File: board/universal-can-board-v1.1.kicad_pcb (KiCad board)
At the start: 2 copper layers, 49.5 x 111.8 mm, 70 parts, among them IC1 ATMEGA328P-A, P1 USB_OTG, P2 CONN_01X08, P3 CONN_01X02, P4 CONN_01X08, P5 CONN_01X08, U1 FT232RL, U2 LM1117-3.3, U3 MCP2515-I/ST, U4 MCP2551-I/SN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

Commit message: Just saved new pcb layout try.
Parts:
- D10, D11, D12, D13, D14, D4, D5, D6, D7, D8, D9, R10, R11, R12, R13, R14, R7, R8, R9, U1, U4: moved to B.Cu
- moved C23 91.0 mm to (244.3, 119.9)
- moved C25 91.0 mm to (245.4, 125.0)
- moved R15 91.0 mm to (238.3, 130.0)
- moved R5 91.0 mm to (246.9, 115.8)
- moved C24 91.0 mm to (239.5, 152.4)
- moved C9 91.0 mm to (251.0, 144.8)
- moved R16 91.0 mm to (234.2, 125.5)
- moved U4 70.2 mm to (145.3, 57.9), turned to 0 degrees
- moved Y2 68.8 mm to (141.7, 68.1), turned to 90 degrees
- moved C5 68.8 mm to (230.1, 95.0)
- moved R2 68.8 mm to (225.0, 101.1)
- moved R4 68.8 mm to (225.0, 96.0)
- moved R3 64.8 mm to (215.4, 46.7)
- moved C21 57.9 mm to (143.3, 97.0), turned to 180 degrees
- moved P4 54.9 mm to (156.0, 80.3), turned to 90 degrees
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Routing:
- net Net-(C20-Pad1): track 92.5 -> 0.00 mm, vias 2 -> 0
- net VCC: track 57.5 -> 0.00 mm, vias 2 -> 0
- net +5V: track 46.3 -> 0.00 mm, vias 1 -> 0
- net Net-(D14-Pad2): track 45.8 -> 0.00 mm
- net Net-(P4-Pad5): track 37.9 -> 0.00 mm, vias 1 -> 0
- net Net-(P4-Pad4): track 29.1 -> 0.00 mm
- net Net-(U3-Pad2): track 16.3 -> 0.00 mm
- net USB_D-: track 15.9 -> 0.00 mm
- net USB_D+: track 15.7 -> 0.00 mm, vias 2 -> 0
- net Net-(U3-Pad9): track 10.9 -> 0.00 mm
- net Net-(U3-Pad1): track 6.75 -> 0.00 mm
- net Net-(U3-Pad8): track 5.24 -> 0.00 mm
- net RESET: track 3.28 -> 0.00 mm
- net Net-(R15-Pad1): track 2.78 -> 0.00 mm
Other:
- board outline removed

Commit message: Moved on with the layout.
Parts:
- C1, C4, R16, R2, R3: moved to B.Cu
- D13, D14, D4: moved to F.Cu
- moved C9 122.0 mm to (138.7, 97.0)
- moved R15 115.8 mm to (152.4, 52.3)
- moved C24 115.2 mm to (136.1, 101.6)
- moved R16 112.5 mm to (148.3, 52.8), turned to 180 degrees
- moved C23 111.1 mm to (148.3, 64.0), turned to 0 degrees
- moved C25 107.7 mm to (149.4, 76.2)
- moved R5 103.4 mm to (145.3, 96.5)
- moved R3 88.0 mm to (144.3, 98.6), turned to 90 degrees
- moved R4 83.0 mm to (144.3, 115.3)
- moved C4 79.7 mm to (145.3, 103.6), turned to 270 degrees
- moved R2 78.3 mm to (146.8, 98.6), turned to 270 degrees
- moved C5 77.9 mm to (152.4, 89.9), turned to 270 degrees
- moved C3 74.9 mm to (138.7, 86.9), turned to 90 degrees
- moved D3 65.6 mm to (150.9, 117.3)
- moved R6 65.4 mm to (158.0, 116.3)
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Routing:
- net IO7: track 0.00 -> 58.2 mm, vias 0 -> 3
- net IO5: track 0.00 -> 52.8 mm, vias 0 -> 5
- net IO6: track 0.00 -> 50.7 mm, vias 0 -> 3
- net Net-(D14-Pad2): track 0.00 -> 50.1 mm, vias 0 -> 1
- net IO4: track 0.00 -> 44.2 mm, vias 0 -> 3
- net VCC: track 0.00 -> 34.2 mm, vias 0 -> 2
- net +5V: track 0.00 -> 33.8 mm
- net IO2: track 0.00 -> 33.1 mm, vias 0 -> 3
- net IO1: track 0.00 -> 27.0 mm, vias 0 -> 3
- net IO0: track 0.00 -> 19.5 mm, vias 0 -> 1
- net CAN_INT: track 0.00 -> 18.0 mm, vias 0 -> 2
- net CAN_SO: track 0.00 -> 13.4 mm, vias 0 -> 2
- net Net-(U3-Pad1): track 0.00 -> 12.6 mm, vias 0 -> 1
- net Net-(C20-Pad1): track 0.00 -> 12.2 mm
- net Net-(U3-Pad2): track 0.00 -> 11.6 mm, vias 0 -> 1
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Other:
- board outline added: 49.3 x 59.4 mm

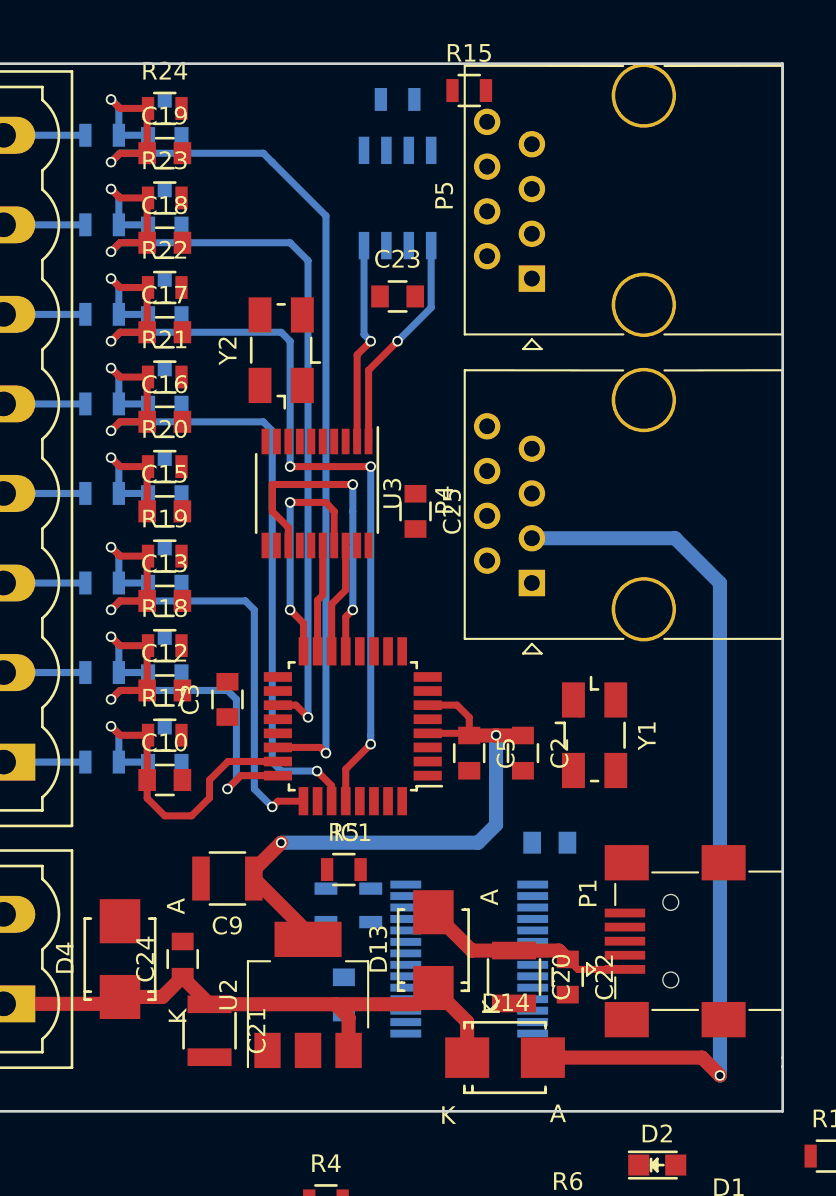
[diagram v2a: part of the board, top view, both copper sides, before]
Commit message: Routing of board v1.1
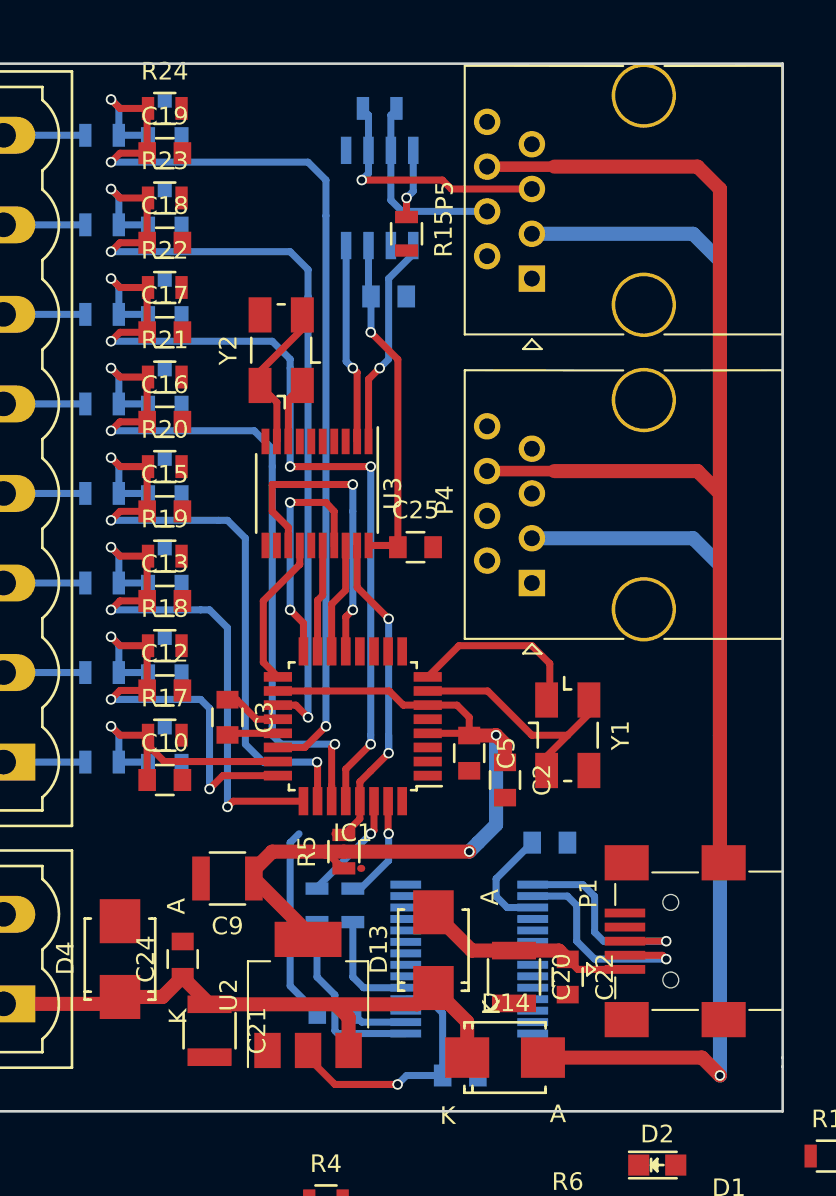
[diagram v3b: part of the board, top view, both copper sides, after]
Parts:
- added C6: 100n, Capacitors_SMD:C_0805, B.Cu at (151.9, 108.2)
- C23: moved to B.Cu
- moved R15 8.87 mm to (148.8, 60.5), turned to 270 degrees
- moved R2 3.05 mm to (143.8, 98.6)
- moved C25 2.03 mm to (149.4, 78.2), turned to 0 degrees
- moved C2 1.83 mm to (154.4, 91.4)
- moved R3 1.52 mm to (145.8, 98.6)
- moved Y1 1.52 mm to (158.0, 88.9)
- moved R16 1.14 mm to (147.3, 53.3)
- moved C4 1.14 mm to (144.8, 104.6), turned to 0 degrees
- moved U4 1.02 mm to (147.3, 58.4)
- moved C3 1.02 mm to (138.7, 87.9), turned to 270 degrees
- moved R5 1.02 mm to (145.3, 95.5), turned to 90 degrees
- moved C23 0.51 mm to (147.8, 64.0)
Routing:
- net GND: track 0.00 -> 68.7 mm
- net VCC: track 34.2 -> 79.1 mm, vias 2 -> 4
- net RESET: track 0.00 -> 30.8 mm, vias 0 -> 2
- net Net-(D14-Pad2): track 50.1 -> 79.3 mm
- net IO3: track 8.75 -> 37.4 mm, vias 1 -> 3
- net Net-(P4-Pad5): track 0.00 -> 14.2 mm, vias 0 -> 1
- net Net-(IC1-Pad7): track 0.00 -> 14.0 mm
- net USB_D-: track 0.00 -> 12.7 mm, vias 0 -> 1
- net USB_D+: track 0.00 -> 12.4 mm, vias 0 -> 1
- net Net-(P4-Pad4): track 0.00 -> 11.1 mm
- net USB_RX: track 0.00 -> 10.7 mm
- net Net-(IC1-Pad8): track 0.80 -> 10.2 mm
- net CAN_SCK: track 0.00 -> 8.66 mm
- net Net-(U3-Pad9): track 0.00 -> 8.57 mm
- net USB_TX: track 0.00 -> 6.37 mm
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
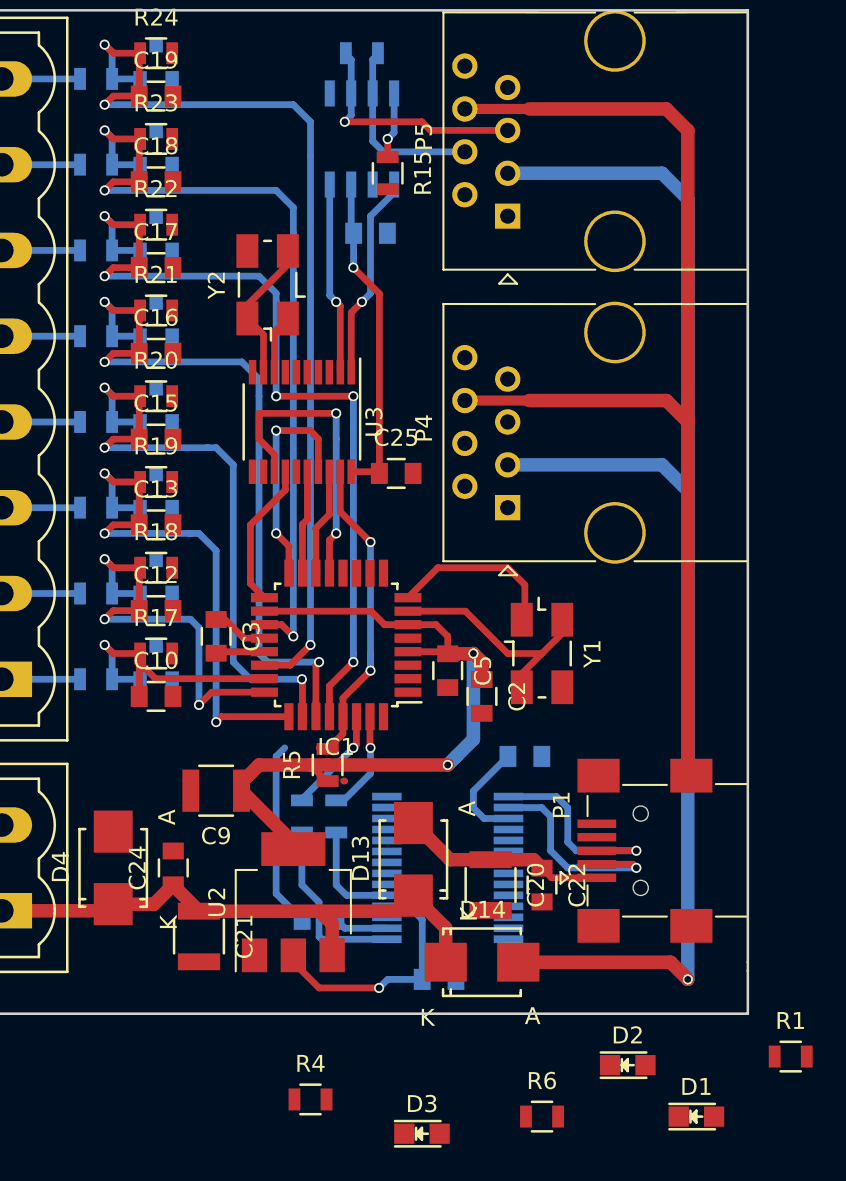
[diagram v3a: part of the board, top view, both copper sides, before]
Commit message: Routing of PCB v1.1. All parts are placed now.
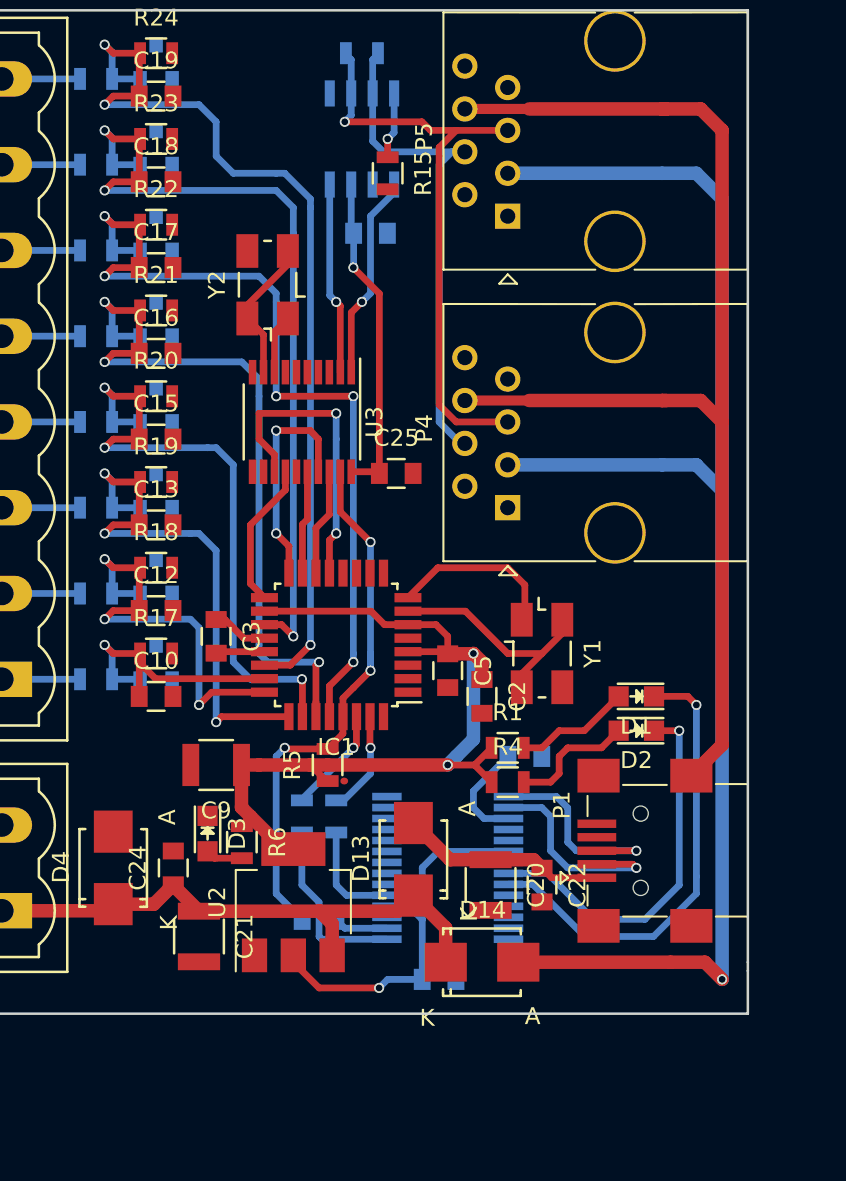
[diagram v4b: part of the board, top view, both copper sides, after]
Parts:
- moved D1 25.1 mm to (163.6, 91.4), turned to 180 degrees
- moved R1 24.8 mm to (156.0, 94.5)
- moved R6 24.1 mm to (140.2, 100.1), turned to 270 degrees
- moved R4 22.1 mm to (156.0, 96.5)
- moved D3 21.8 mm to (138.2, 99.6), turned to 270 degrees
- moved D2 19.8 mm to (163.6, 93.5), turned to 180 degrees
- moved C9 1.52 mm to (138.7, 95.5)
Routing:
- net Net-(D1-Pad1): track 0.00 -> 27.4 mm, vias 0 -> 1
- net Net-(D2-Pad1): track 0.00 -> 22.7 mm, vias 0 -> 1
- net Net-(P4-Pad5): track 14.2 -> 35.4 mm
- net Net-(P4-Pad4): track 11.1 -> 30.2 mm
- net VCC: track 79.1 -> 94.2 mm
- net Net-(D2-Pad2): track 0.00 -> 7.48 mm
- net Net-(D1-Pad2): track 0.00 -> 6.88 mm
- net Net-(D14-Pad2): track 79.3 -> 85.4 mm
- net GND: track 68.7 -> 74.2 mm
- net RESET: track 30.8 -> 33.3 mm, vias 2 -> 3
- net Net-(D3-Pad2): track 0.00 -> 2.20 mm
- net IO7: track 57.8 -> 56.3 mm

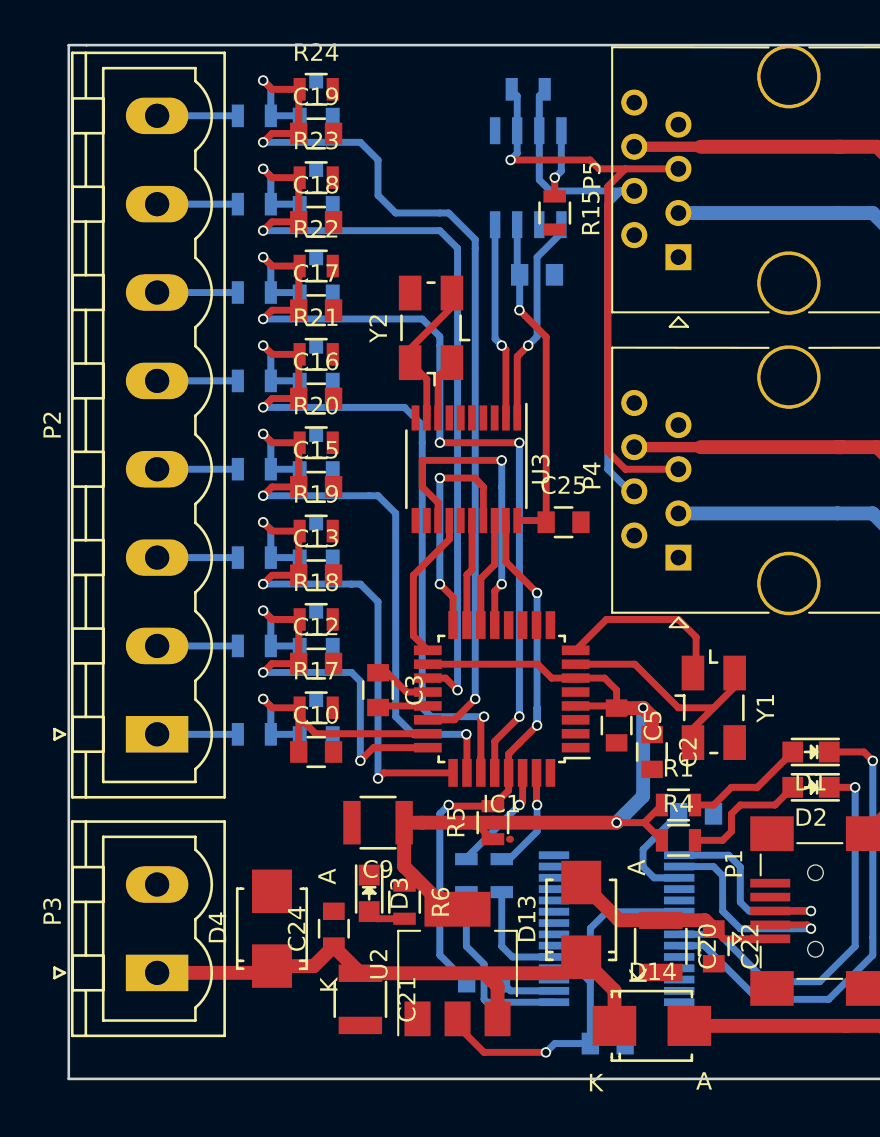
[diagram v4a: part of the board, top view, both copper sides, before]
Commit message: Updated board layout.
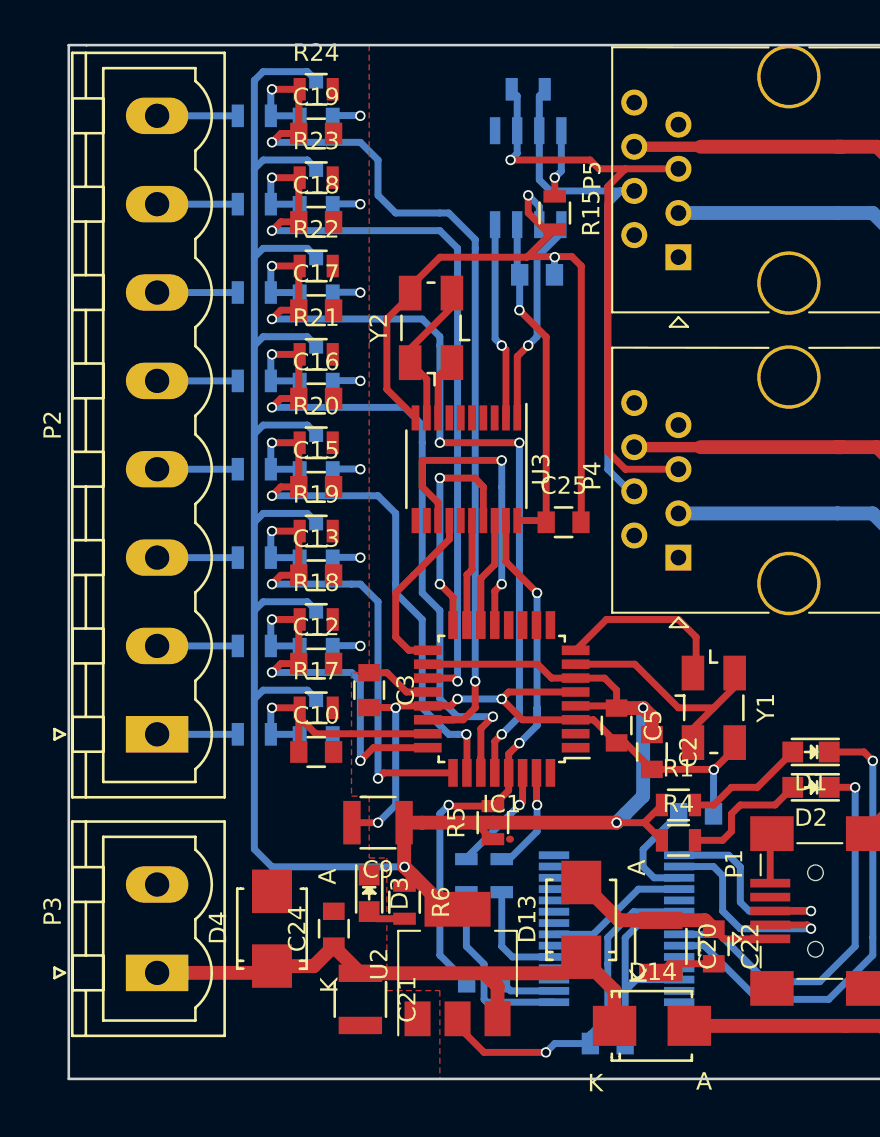
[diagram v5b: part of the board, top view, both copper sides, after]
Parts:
- moved C3 0.51 mm to (138.2, 87.9)
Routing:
- net GND: track 74.2 -> 192.2 mm, vias 0 -> 14
- net VCC: track 94.2 -> 176.2 mm, vias 4 -> 5
- net IO3: track 37.4 -> 34.0 mm
- net IO6: track 50.0 -> 47.0 mm
- net IO4: track 44.8 -> 42.3 mm
- net IO1: track 25.6 -> 23.3 mm
- net IO2: track 32.6 -> 30.4 mm
- net IO5: track 51.8 -> 49.6 mm
- net CAN_SCK: track 8.66 -> 10.1 mm
- net IO0: track 17.1 -> 15.8 mm
- added copper zone on F.Cu, net GND
